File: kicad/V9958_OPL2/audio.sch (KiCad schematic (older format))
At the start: 16 parts

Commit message: stuff
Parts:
- C11, C14: renamed from C?; footprint Capacitors_ThroughHole:C_Radial_D6.3_L11.2_P2.5 -> Capacitors_ThroughHole:CP_Radial_D6.3mm_P2.50mm
- C12, C13: renamed from C?; footprint Capacitors_ThroughHole:C_Disc_D3_P2.5 -> Capacitors_ThroughHole:C_Disc_D3.0mm_W1.6mm_P2.50mm
- J1: renamed from J?; value Conn_Coaxial -> Audio; footprint (none) -> w_conn_av:rca_black
- U11: renamed from U?; footprint (none) -> Housings_DIP:DIP-14_W7.62mm_Socket_LongPads
- gave numbers to parts that had none: 7
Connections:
- net at C11.1, U10.7 (RB): now also U11.5 (+); no longer U11.3 (+)
- net at R2.2, R4.1, U10.8 (MP): now also U11.6 (-), U11.7; no longer U11.1, U11.2 (-)
- net at C12.2, R3.2: now also U11.10 (+); no longer U11.3 (+)
- net at C14.1, R5.2, R6.2: now also U11.14; no longer U11.1
- net at R4.2, R5.1: now also U11.13 (-); no longer U11.2 (-)
- net AUDIO_OUT: now reaches C14.2, J1.1 (In)
- new net: C13.1, U11.12 (+), U11.8, U11.9 (-)
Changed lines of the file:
@@
 LIBS:steckschwein
 LIBS:yamaha_opl
+LIBS:w_connectors
 LIBS:v9958-cache
 EELAYER 25 0
@@
 $EndDescr
 $Comp
-L Y3014B U?
+L Y3014B U10
 U 1 1 5BE25F45
 P 3850 3450
-F 0 "U?" H 3850 3500 60  0000 C CNN
+F 0 "U10" H 3850 3500 60  0000 C CNN
 F 1 "Y3014B" H 3850 3400 60  0000 C CNN
 F 2 "Housings_DIP:DIP-8_W7.62mm_LongPads" H 3850 3450 60  0001 C CNN
@@
 	2850 3450 3050 3450
 $Comp
-L LM324 U?
-U 1 1 5BE25F4F
+L LM324 U11
+U 2 1 5BE25F4F
 P 5200 4050
-F 0 "U?" H 5200 4250 50  0000 L CNN
+F 0 "U11" H 5200 4250 50  0000 L CNN
 F 1 "LM324" H 5200 3850 50  0000 L CNN
-F 2 "" H 5150 4150 50  0001 C CNN
+F 2 "Housings_DIP:DIP-14_W7.62mm_Socket_LongPads" H 5150 4150 50  0001 C CNN
 F 3 "" H 5250 4250 50  0001 C CNN
-	1    5200 4050
+	2    5200 4050
 	1    0    0    -1
 $EndComp
@@
 Connection ~ 4850 4600
 $Comp
-L CP C?
+L CP C11
 U 1 1 5BE25F5F
 P 4650 4200
-F 0 "C?" H 4675 4300 50  0000 L CNN
+F 0 "C11" H 4675 4300 50  0000 L CNN
 F 1 "10µF" H 4675 4100 50  0000 L CNN
-F 2 "Capacitors_ThroughHole:C_Radial_D6.3_L11.2_P2.5" H 4688 4050 50  0001 C CNN
+F 2 "Capacitors_ThroughHole:CP_Radial_D6.3mm_P2.50mm" H 4688 4050 50  0001 C CNN
 F 3 "" H 4650 4200 50  0000 C CNN
 	1    4650 4200
@@
 Connection ~ 4650 3950
 $Comp
-L GND-RESCUE-v9958 #PWR?
+L GND-RESCUE-v9958 #PWR025
 U 1 1 5BE25F68
 P 4650 4400
-F 0 "#PWR?" H 4650 4400 30  0001 C CNN
+F 0 "#PWR025" H 4650 4400 30  0001 C CNN
 F 1 "GND" H 4650 4330 30  0001 C CNN
 F 2 "" H 4650 4400 60  0000 C CNN
@@
 	4650 4400 4650 4350
 $Comp
-L R-RESCUE-v9958 R?
+L R-RESCUE-v9958 R2
 U 1 1 5BE25F6F
 P 5800 4400
-F 0 "R?" V 5880 4400 40  0000 C CNN
+F 0 "R2" V 5880 4400 40  0000 C CNN
 F 1 "4K7" V 5807 4401 40  0000 C CNN
 F 2 "Discret:R3" V 5730 4400 30  0001 C CNN
@@
 Connection ~ 5550 4050
 $Comp
-L GND-RESCUE-v9958 #PWR?
+L GND-RESCUE-v9958 #PWR026
 U 1 1 5BE25F77
 P 5800 4750
-F 0 "#PWR?" H 5800 4750 30  0001 C CNN
+F 0 "#PWR026" H 5800 4750 30  0001 C CNN
 F 1 "GND" H 5800 4680 30  0001 C CNN
 F 2 "" H 5800 4750 60  0000 C CNN
@@
 	5800 4650 5800 4750
 $Comp
-L LM324 U?
+L LM324 U11
 U 1 1 5BE25F7E
 P 5100 2850
-F 0 "U?" H 5100 3050 50  0000 L CNN
+F 0 "U11" H 5100 3050 50  0000 L CNN
 F 1 "LM324" H 5100 2650 50  0000 L CNN
-F 2 "" H 5050 2950 50  0001 C CNN
+F 2 "Housings_DIP:DIP-14_W7.62mm_Socket_LongPads" H 5050 2950 50  0001 C CNN
 F 3 "" H 5150 3050 50  0001 C CNN
 	1    5100 2850
@@
 $EndComp
 $Comp
-L GND-RESCUE-v9958 #PWR?
+L GND-RESCUE-v9958 #PWR027
 U 1 1 5BE25F85
 P 5100 4400
-F 0 "#PWR?" H 5100 4400 30  0001 C CNN
+F 0 "#PWR027" H 5100 4400 30  0001 C CNN
 F 1 "GND" H 5100 4330 30  0001 C CNN
 F 2 "" H 5100 4400 60  0000 C CNN
@@
 $EndComp
 $Comp
-L VCC #PWR?
+L VCC #PWR028
 U 1 1 5BE25F8B
 P 5100 3600
-F 0 "#PWR?" H 5100 3700 30  0001 C CNN
+F 0 "#PWR028" H 5100 3700 30  0001 C CNN
 F 1 "VCC" H 5100 3700 30  0000 C CNN
 F 2 "" H 5100 3600 60  0000 C CNN
@@
 	5400 2850 5550 2850
 $Comp
-L GND-RESCUE-v9958 #PWR?
+L GND-RESCUE-v9958 #PWR029
 U 1 1 5BE25F99
 P 5000 3200
-F 0 "#PWR?" H 5000 3200 30  0001 C CNN
+F 0 "#PWR029" H 5000 3200 30  0001 C CNN
 F 1 "GND" H 5000 3130 30  0001 C CNN
 F 2 "" H 5000 3200 60  0000 C CNN
@@
 	5000 3150 5000 3200
 $Comp
-L VCC #PWR?
+L VCC #PWR030
 U 1 1 5BE25FA0
 P 8650 3600
-F 0 "#PWR?" H 8650 3700 30  0001 C CNN
+F 0 "#PWR030" H 8650 3700 30  0001 C CNN
 F 1 "VCC" H 8650 3700 30  0000 C CNN
 F 2 "" H 8650 3600 60  0000 C CNN
@@
 	8650 3600 8650 3650
 $Comp
-L LM324 U?
-U 1 1 5BE25FA7
+L LM324 U11
+U 3 1 5BE25FA7
 P 7350 2950
-F 0 "U?" H 7350 3150 50  0000 L CNN
+F 0 "U11" H 7350 3150 50  0000 L CNN
 F 1 "LM324" H 7350 2750 50  0000 L CNN
-F 2 "" H 7300 3050 50  0001 C CNN
+F 2 "Housings_DIP:DIP-14_W7.62mm_Socket_LongPads" H 7300 3050 50  0001 C CNN
 F 3 "" H 7400 3150 50  0001 C CNN
-	1    7350 2950
-	1    0    0    -1
-$EndComp
-$Comp
-L R-RESCUE-v9958 R?
+	3    7350 2950
+	1    0    0    -1
+$EndComp
+$Comp
+L R-RESCUE-v9958 R1
 U 1 1 5BE25FAE
 P 5800 2850
-F 0 "R?" V 5880 2850 40  0000 C CNN
+F 0 "R1" V 5880 2850 40  0000 C CNN
 F 1 "33K" V 5807 2851 40  0000 C CNN
 F 2 "Discret:R3" V 5730 2850 30  0001 C CNN
@@
 $EndComp
 $Comp
-L R-RESCUE-v9958 R?
+L R-RESCUE-v9958 R3
 U 1 1 5BE25FB5
 P 6400 2850
-F 0 "R?" V 6480 2850 40  0000 C CNN
+F 0 "R3" V 6480 2850 40  0000 C CNN
 F 1 "33K" V 6407 2851 40  0000 C CNN
 F 2 "Discret:R3" V 6330 2850 30  0001 C CNN
@@
 	6650 2850 7050 2850
 $Comp
-L C C?
+L C C13
 U 1 1 5BE25FBE
 P 6900 2350
-F 0 "C?" H 6925 2450 50  0000 L CNN
+F 0 "C13" H 6925 2450 50  0000 L CNN
 F 1 "470p" H 6925 2250 50  0000 L CNN
-F 2 "Capacitors_ThroughHole:C_Disc_D3_P2.5" H 6938 2200 50  0001 C CNN
+F 2 "Capacitors_ThroughHole:C_Disc_D3.0mm_W1.6mm_P2.50mm" H 6938 2200 50  0001 C CNN
 F 3 "" H 6900 2350 50  0001 C CNN
 	1    6900 2350
@@
 Connection ~ 7850 2950
 $Comp
-L C C?
+L C C12
 U 1 1 5BE25FCF
 P 6750 3200
-F 0 "C?" H 6775 3300 50  0000 L CNN
+F 0 "C12" H 6775 3300 50  0000 L CNN
 F 1 "470p" H 6775 3100 50  0000 L CNN
-F 2 "Capacitors_ThroughHole:C_Disc_D3_P2.5" H 6788 3050 50  0001 C CNN
+F 2 "Capacitors_ThroughHole:C_Disc_D3.0mm_W1.6mm_P2.50mm" H 6788 3050 50  0001 C CNN
 F 3 "" H 6750 3200 50  0001 C CNN
 	1    6750 3200
@@
 $EndComp
 $Comp
-L GND-RESCUE-v9958 #PWR?
+L GND-RESCUE-v9958 #PWR031
 U 1 1 5BE25FD7
 P 7250 3500
-F 0 "#PWR?" H 7250 3500 30  0001 C CNN
+F 0 "#PWR031" H 7250 3500 30  0001 C CNN
 F 1 "GND" H 7250 3430 30  0001 C CNN
 F 2 "" H 7250 3500 60  0000 C CNN
@@
 $EndComp
 $Comp
-L GND-RESCUE-v9958 #PWR?
+L GND-RESCUE-v9958 #PWR032
 U 1 1 5BE25FDD
 P 6750 3500
-F 0 "#PWR?" H 6750 3500 30  0001 C CNN
+F 0 "#PWR032" H 6750 3500 30  0001 C CNN
 F 1 "GND" H 6750 3430 30  0001 C CNN
 F 2 "" H 6750 3500 60  0000 C CNN
@@
 	7250 3250 7250 3500
 $Comp
-L VCC #PWR?
+L VCC #PWR033
 U 1 1 5BE25FE5
 P 5000 2500
-F 0 "#PWR?" H 5000 2600 30  0001 C CNN
+F 0 "#PWR033" H 5000 2600 30  0001 C CNN
 F 1 "VCC" H 5000 2600 30  0000 C CNN
 F 2 "" H 5000 2500 60  0000 C CNN
@@
 	5000 2500 5000 2550
 $Comp
-L VCC #PWR?
+L VCC #PWR034
 U 1 1 5BE25FEC
 P 7250 2550
-F 0 "#PWR?" H 7250 2650 30  0001 C CNN
+F 0 "#PWR034" H 7250 2650 30  0001 C CNN
 F 1 "VCC" H 7250 2650 30  0000 C CNN
 F 2 "" H 7250 2550 60  0000 C CNN
@@
 	7250 2550 7250 2650
 $Comp
-L LM324 U?
-U 1 1 5BE25FF3
+L LM324 U11
+U 4 1 5BE25FF3
 P 8750 3950
-F 0 "U?" H 8750 4150 50  0000 L CNN
+F 0 "U11" H 8750 4150 50  0000 L CNN
 F 1 "LM324" H 8750 3750 50  0000 L CNN
-F 2 "" H 8700 4050 50  0001 C CNN
+F 2 "Housings_DIP:DIP-14_W7.62mm_Socket_LongPads" H 8700 4050 50  0001 C CNN
 F 3 "" H 8800 4150 50  0001 C CNN
-	1    8750 3950
-	1    0    0    -1
-$EndComp
-$Comp
-L R-RESCUE-v9958 R?
+	4    8750 3950
+	1    0    0    -1
+$EndComp
+$Comp
+L R-RESCUE-v9958 R4
 U 1 1 5BE25FFA
 P 7350 4050
-F 0 "R?" V 7430 4050 40  0000 C CNN
+F 0 "R4" V 7430 4050 40  0000 C CNN
 F 1 "15K" V 7357 4051 40  0000 C CNN
 F 2 "Discret:R3" V 7280 4050 30  0001 C CNN
@@
 	7600 4050 8450 4050
 $Comp
-L R-RESCUE-v9958 R?
+L R-RESCUE-v9958 R6
 U 1 1 5BE26004
 P 9500 4800
-F 0 "R?" V 9580 4800 40  0000 C CNN
+F 0 "R6" V 9580 4800 40  0000 C CNN
 F 1 "4K7" V 9507 4801 40  0000 C CNN
 F 2 "Discret:R3" V 9430 4800 30  0001 C CNN
@@
 $EndComp
 $Comp
-L GND-RESCUE-v9958 #PWR?
+L GND-RESCUE-v9958 #PWR035
 U 1 1 5BE2600B
 P 9500 5200
-F 0 "#PWR?" H 9500 5200 30  0001 C CNN
+F 0 "#PWR035" H 9500 5200 30  0001 C CNN
 F 1 "GND" H 9500 5130 30  0001 C CNN
 F 2 "" H 9500 5200 60  0000 C CNN
@@
 Connection ~ 7850 4050
 $Comp
-L R-RESCUE-v9958 R?
+L R-RESCUE-v9958 R5
 U 1 1 5BE26016
 P 8300 4500
-F 0 "R?" V 8380 4500 40  0000 C CNN
+F 0 "R5" V 8380 4500 40  0000 C CNN
 F 1 "27K" V 8307 4501 40  0000 C CNN
 F 2 "Discret:R3" V 8230 4500 30  0001 C CNN
@@
 	7850 4500 8050 4500
 $Comp
-L CP C?
+L CP C14
 U 1 1 5BE2601E
 P 9900 3950
-F 0 "C?" H 9925 4050 50  0000 L CNN
+F 0 "C14" H 9925 4050 50  0000 L CNN
 F 1 "10µF" H 9925 3850 50  0000 L CNN
-F 2 "Capacitors_ThroughHole:C_Radial_D6.3_L11.2_P2.5" H 9938 3800 50  0001 C CNN
+F 2 "Capacitors_ThroughHole:CP_Radial_D6.3mm_P2.50mm" H 9938 3800 50  0001 C CNN
 F 3 "" H 9900 3950 50  0000 C CNN
 	1    9900 3950
@@
 	5100 4350 5100 4400
 $Comp
-L GND-RESCUE-v9958 #PWR?
+L GND-RESCUE-v9958 #PWR036
 U 1 1 5BE26029
 P 8650 4400
-F 0 "#PWR?" H 8650 4400 30  0001 C CNN
+F 0 "#PWR036" H 8650 4400 30  0001 C CNN
 F 1 "GND" H 8650 4330 30  0001 C CNN
 F 2 "" H 8650 4400 60  0000 C CNN
@@
 SD
 $Comp
-L Conn_Coaxial J?
+L Conn_Coaxial J1
 U 1 1 5BE2854B
 P 10400 3950
-F 0 "J?" H 10410 4070 50  0000 C CNN
-F 1 "Conn_Coaxial" V 10515 3950 50  0000 C CNN
-F 2 "" H 10400 3950 50  0001 C CNN
+F 0 "J1" H 10410 4070 50  0000 C CNN
+F 1 "Audio" V 10515 3950 50  0000 C CNN
+F 2 "w_conn_av:rca_black" H 10400 3950 50  0001 C CNN
 F 3 "" H 10400 3950 50  0001 C CNN
 	1    10400 3950
@@
 	10050 3950 10250 3950
 $Comp
-L GND-RESCUE-v9958 #PWR?
+L GND-RESCUE-v9958 #PWR037
 U 1 1 5BE28690
 P 10400 4450
-F 0 "#PWR?" H 10400 4450 30  0001 C CNN
+F 0 "#PWR037" H 10400 4450 30  0001 C CNN
 F 1 "GND" H 10400 4380 30  0001 C CNN
 F 2 "" H 10400 4450 60  0000 C CNN
@@
 Wire Wire Line
 	10400 4150 10400 4450
+Wire Wire Line
+	10150 3700 10150 3950
+Connection ~ 10150 3950
+Text HLabel 10150 3700 1    60   Output ~ 0
+AUDIO_OUT
 $EndSCHEMATC

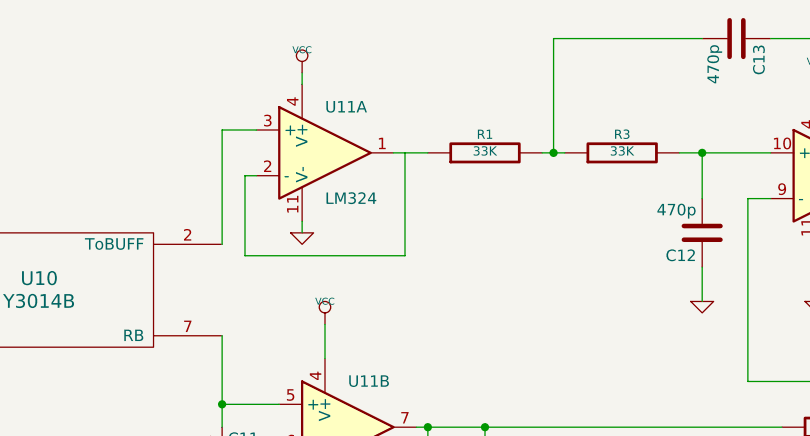
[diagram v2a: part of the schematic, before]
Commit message: DRC fixes, filled areas
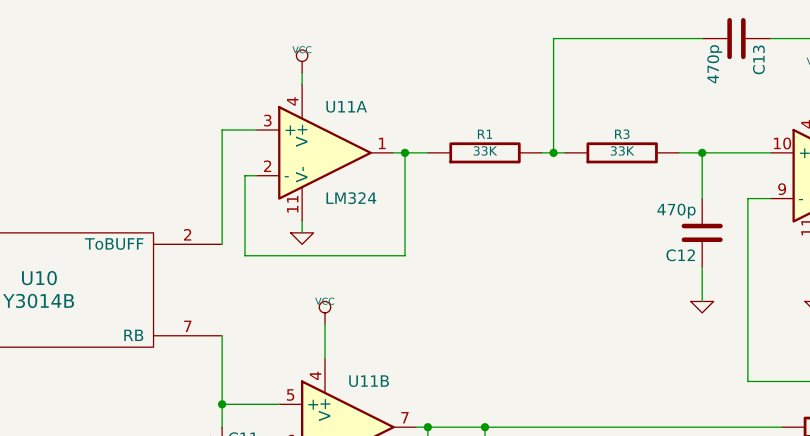
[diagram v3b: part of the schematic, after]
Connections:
- net at R1.1, U11.1: now also U11.2 (-)
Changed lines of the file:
@@
 Text HLabel 10150 3700 1    60   Output ~ 0
 AUDIO_OUT
+Connection ~ 5450 2850
 $EndSCHEMATC

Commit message: small improvements
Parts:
- U11: footprint Housings_DIP:DIP-14_W7.62mm_Socket_LongPads -> Housings_DIP:DIP-14_W7.62mm_LongPads
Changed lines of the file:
@@
 F 0 "U11" H 5200 4250 50  0000 L CNN
 F 1 "LM324" H 5200 3850 50  0000 L CNN
-F 2 "Housings_DIP:DIP-14_W7.62mm_Socket_LongPads" H 5150 4150 50  0001 C CNN
+F 2 "Housings_DIP:DIP-14_W7.62mm_LongPads" H 5150 4150 50  0001 C CNN
 F 3 "" H 5250 4250 50  0001 C CNN
 	2    5200 4050
@@
 F 0 "U11" H 5100 3050 50  0000 L CNN
 F 1 "LM324" H 5100 2650 50  0000 L CNN
-F 2 "Housings_DIP:DIP-14_W7.62mm_Socket_LongPads" H 5050 2950 50  0001 C CNN
+F 2 "Housings_DIP:DIP-14_W7.62mm_LongPads" H 5050 2950 50  0001 C CNN
 F 3 "" H 5150 3050 50  0001 C CNN
 	1    5100 2850
@@
 F 0 "U11" H 7350 3150 50  0000 L CNN
 F 1 "LM324" H 7350 2750 50  0000 L CNN
-F 2 "Housings_DIP:DIP-14_W7.62mm_Socket_LongPads" H 7300 3050 50  0001 C CNN
+F 2 "Housings_DIP:DIP-14_W7.62mm_LongPads" H 7300 3050 50  0001 C CNN
 F 3 "" H 7400 3150 50  0001 C CNN
 	3    7350 2950
@@
 F 0 "U11" H 8750 4150 50  0000 L CNN
 F 1 "LM324" H 8750 3750 50  0000 L CNN
-F 2 "Housings_DIP:DIP-14_W7.62mm_Socket_LongPads" H 8700 4050 50  0001 C CNN
+F 2 "Housings_DIP:DIP-14_W7.62mm_LongPads" H 8700 4050 50  0001 C CNN
 F 3 "" H 8800 4150 50  0001 C CNN
 	4    8750 3950

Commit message: correct rca footprint, layers setup
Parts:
- J1: footprint w_conn_av:rca_black -> misc:rca
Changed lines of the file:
@@
 F 0 "J1" H 10410 4070 50  0000 C CNN
 F 1 "Audio" V 10515 3950 50  0000 C CNN
-F 2 "w_conn_av:rca_black" H 10400 3950 50  0001 C CNN
+F 2 "misc:rca" H 10400 3950 50  0001 C CNN
 F 3 "" H 10400 3950 50  0001 C CNN
 	1    10400 3950

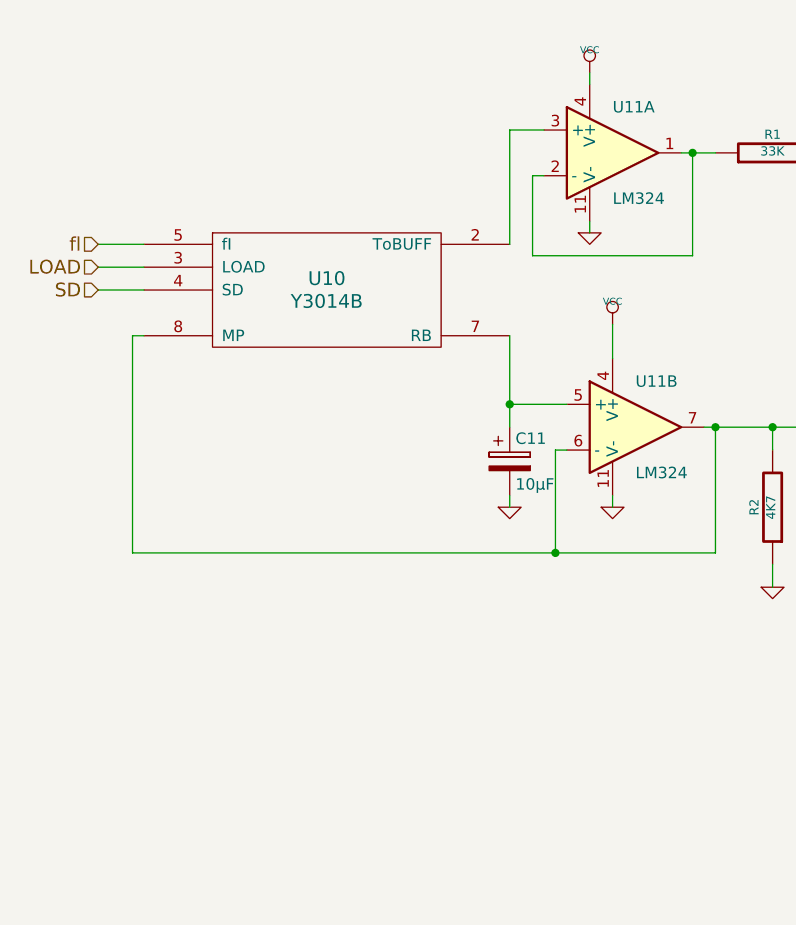
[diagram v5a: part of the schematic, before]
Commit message: more cap for opamp, small routing fixes
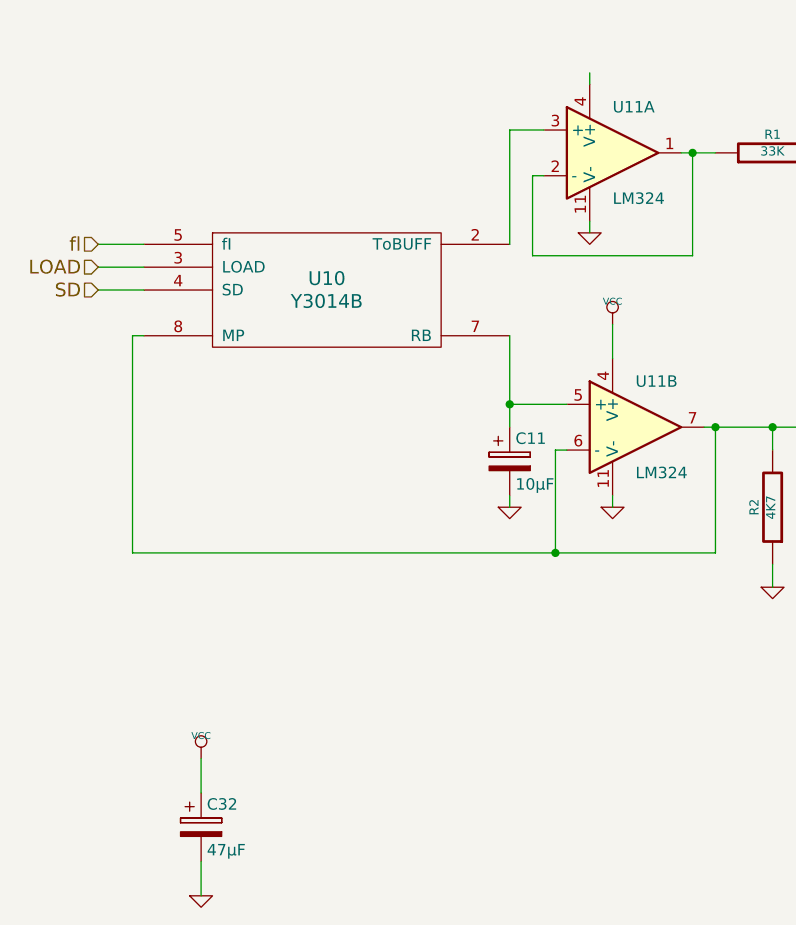
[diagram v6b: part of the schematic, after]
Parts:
- added C32: 47µF, Capacitors_ThroughHole:CP_Radial_D6.3mm_P2.50mm, symbol CP
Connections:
- net GND: now also C32.2
- net VCC: now also C32.1; no longer U11.4 (V+)
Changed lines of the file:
@@
 Wire Wire Line
 	7250 3250 7250 3500
-$Comp
-L VCC #PWR033
-U 1 1 5BE25FE5
-P 5000 2500
-F 0 "#PWR033" H 5000 2600 30  0001 C CNN
-F 1 "VCC" H 5000 2600 30  0000 C CNN
-F 2 "" H 5000 2500 60  0000 C CNN
-F 3 "" H 5000 2500 60  0000 C CNN
-	1    5000 2500
-	1    0    0    -1
-$EndComp
 Wire Wire Line
 	5000 2500 5000 2550
@@
 AUDIO_OUT
 Connection ~ 5450 2850
+$Comp
+L VCC #PWR038
+U 1 1 5C094DEB
+P 3300 5500
+F 0 "#PWR038" H 3300 5600 30  0001 C CNN
+F 1 "VCC" H 3300 5600 30  0000 C CNN
+F 2 "" H 3300 5500 60  0000 C CNN
+F 3 "" H 3300 5500 60  0000 C CNN
+	1    3300 5500
+	1    0    0    -1
+$EndComp
+$Comp
+L GND-RESCUE-v9958 #PWR039
+U 1 1 5C094E26
+P 3300 6100
+F 0 "#PWR039" H 3300 6100 30  0001 C CNN
+F 1 "GND" H 3300 6030 30  0001 C CNN
+F 2 "" H 3300 6100 60  0000 C CNN
+F 3 "" H 3300 6100 60  0000 C CNN
+	1    3300 6100
+	1    0    0    -1
+$EndComp
+$Comp
+L CP C32
+U 1 1 5C094F4B
+P 3300 5800
+F 0 "C32" H 3325 5900 50  0000 L CNN
+F 1 "47µF" H 3325 5700 50  0000 L CNN
+F 2 "Capacitors_ThroughHole:CP_Radial_D6.3mm_P2.50mm" H 3338 5650 50  0001 C CNN
+F 3 "" H 3300 5800 50  0000 C CNN
+	1    3300 5800
+	1    0    0    -1
+$EndComp
+Wire Wire Line
+	3300 5500 3300 5650
+Wire Wire Line
+	3300 5950 3300 6100
 $EndSCHEMATC
